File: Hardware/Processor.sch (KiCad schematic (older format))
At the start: 24 parts, among them J1 ICSP-CORTEX, J3 CONN-9, U6 STM32L100RBT6, X1 8MHz

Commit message: Component associations
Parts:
- removed R?: R, ~, symbol R
- added R18: 10k, RESC1608, symbol R
- gave numbers to parts that had none: 7
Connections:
- net +3.3V: now also R18.2
- net VLCD: now also R18.1
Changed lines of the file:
@@
 $EndComp
 $Comp
-L VCOM #PWR38
+L VCOM #PWR50
 U 1 1 52B50CC7
 P 9300 5500
-F 0 "#PWR38" H 9300 5700 40  0001 C CNN
+F 0 "#PWR50" H 9300 5700 40  0001 C CNN
 F 1 "VCOM" H 9300 5650 40  0000 C CNN
 F 2 "" H 9300 5500 60  0000 C CNN
@@
 LED0
 Wire Wire Line
-	2800 5100 2800 5200
-Wire Wire Line
-	2800 5200 2800 5300
-Wire Wire Line
-	2100 5100 2100 5200
-Wire Wire Line
-	2100 5200 2100 5300
+	2800 5100 2800 5300
+Wire Wire Line
+	2100 5100 2100 5300
 Wire Wire Line
 	2200 5200 2100 5200
@@
 	5700 3800 5600 3800
 Wire Wire Line
-	4400 3500 4400 3600
-Wire Wire Line
-	4400 3600 4400 3800
-Wire Wire Line
-	4400 3800 4400 4300
-Wire Wire Line
-	4400 4300 4400 4500
+	4400 3500 4400 4500
 Wire Wire Line
 	4400 4500 4500 4500
@@
 	2100 2200 2300 2200
 $Comp
-L C C?
+L C C50
 U 1 1 5411C9AD
 P 4300 6850
-F 0 "C?" H 4350 7000 60  0000 L CNN
+F 0 "C50" H 4350 7000 60  0000 L CNN
 F 1 "0.1uF" H 4350 6700 60  0000 L CNN
 F 2 "CAPC1608" H 4300 6850 60  0001 C CNN
@@
 $EndComp
 $Comp
-L C C?
+L C C48
 U 1 1 5411CA70
 P 1600 6850
-F 0 "C?" H 1650 7000 60  0000 L CNN
+F 0 "C48" H 1650 7000 60  0000 L CNN
 F 1 "1uF" H 1650 6700 60  0000 L CNN
 F 2 "CAPC1608" H 1600 6850 60  0001 C CNN
@@
 $EndComp
 $Comp
-L C C?
+L C C47
 U 1 1 5411CA9D
 P 1100 6850
-F 0 "C?" H 1150 7000 60  0000 L CNN
+F 0 "C47" H 1150 7000 60  0000 L CNN
 F 1 "0.1uF" H 1150 6700 60  0000 L CNN
 F 2 "CAPC1608" H 1100 6850 60  0001 C CNN
@@
 $EndComp
 $Comp
-L +3.3V #PWR?
+L +3.3V #PWR039
 U 1 1 5411CAA5
 P 2300 6400
-F 0 "#PWR?" H 2300 6360 30  0001 C CNN
+F 0 "#PWR039" H 2300 6360 30  0001 C CNN
 F 1 "+3.3V" H 2300 6510 30  0000 C CNN
 F 2 "" H 2300 6400 60  0000 C CNN
@@
 $EndComp
 Wire Wire Line
-	2300 6400 2300 6500
-Wire Wire Line
-	2300 6500 2300 6600
-$Comp
-L GND #PWR?
+	2300 6400 2300 6600
+$Comp
+L GND #PWR040
 U 1 1 5411CAE0
 P 2300 7200
-F 0 "#PWR?" H 2300 7200 30  0001 C CNN
+F 0 "#PWR040" H 2300 7200 30  0001 C CNN
 F 1 "GND" H 2300 7130 30  0001 C CNN
 F 2 "" H 2300 7200 60  0000 C CNN
@@
 $EndComp
 $Comp
-L GND #PWR?
+L GND #PWR041
 U 1 1 5411CAEF
 P 2800 7200
-F 0 "#PWR?" H 2800 7200 30  0001 C CNN
+F 0 "#PWR041" H 2800 7200 30  0001 C CNN
 F 1 "GND" H 2800 7130 30  0001 C CNN
 F 2 "" H 2800 7200 60  0000 C CNN
@@
 $EndComp
 $Comp
-L GND #PWR?
+L GND #PWR042
 U 1 1 5411CAFE
 P 3300 7200
-F 0 "#PWR?" H 3300 7200 30  0001 C CNN
+F 0 "#PWR042" H 3300 7200 30  0001 C CNN
 F 1 "GND" H 3300 7130 30  0001 C CNN
 F 2 "" H 3300 7200 60  0000 C CNN
@@
 $EndComp
 $Comp
-L GND #PWR?
+L GND #PWR043
 U 1 1 5411CB0D
 P 3800 7200
-F 0 "#PWR?" H 3800 7200 30  0001 C CNN
+F 0 "#PWR043" H 3800 7200 30  0001 C CNN
 F 1 "GND" H 3800 7130 30  0001 C CNN
 F 2 "" H 3800 7200 60  0000 C CNN
@@
 $EndComp
 $Comp
-L GND #PWR?
+L GND #PWR044
 U 1 1 5411CB1C
 P 4300 7200
-F 0 "#PWR?" H 4300 7200 30  0001 C CNN
+F 0 "#PWR044" H 4300 7200 30  0001 C CNN
 F 1 "GND" H 4300 7130 30  0001 C CNN
 F 2 "" H 4300 7200 60  0000 C CNN
@@
 $EndComp
 $Comp
-L GND #PWR?
+L GND #PWR045
 U 1 1 5411CB2B
 P 1600 7200
-F 0 "#PWR?" H 1600 7200 30  0001 C CNN
+F 0 "#PWR045" H 1600 7200 30  0001 C CNN
 F 1 "GND" H 1600 7130 30  0001 C CNN
 F 2 "" H 1600 7200 60  0000 C CNN
@@
 $EndComp
 $Comp
-L GND #PWR?
+L GND #PWR046
 U 1 1 5411CB3A
 P 1100 7200
-F 0 "#PWR?" H 1100 7200 30  0001 C CNN
+F 0 "#PWR046" H 1100 7200 30  0001 C CNN
 F 1 "GND" H 1100 7130 30  0001 C CNN
 F 2 "" H 1100 7200 60  0000 C CNN
@@
 $EndComp
 Wire Wire Line
-	1100 6400 1100 6500
-Wire Wire Line
-	1100 6500 1100 6600
+	1100 6400 1100 6600
 Connection ~ 2300 6500
 Wire Wire Line
@@
 	4300 7100 4300 7200
 $Comp
-L R R?
-U 1 1 5411CE1B
-P 4650 6500
-F 0 "R?" H 4650 6600 50  0000 C CNN
-F 1 "R" H 4650 6500 50  0000 C CNN
-F 2 "~" H 4650 6500 60  0000 C CNN
-F 3 "~" H 4650 6500 60  0000 C CNN
-F 4 "W" H 4650 6400 50  0001 C CNN "Power"
-F 5 "%" H 4650 6300 50  0001 C CNN "Tolerance"
-	1    4650 6500
-	1    0    0    -1
-$EndComp
-$Comp
-L C C?
+L C C51
 U 1 1 5411CE39
 P 5000 6850
-F 0 "C?" H 5050 7000 60  0000 L CNN
+F 0 "C51" H 5050 7000 60  0000 L CNN
 F 1 "0.1uF" H 5050 6700 60  0000 L CNN
 F 2 "CAPC1608" H 5000 6850 60  0001 C CNN
@@
 Connection ~ 4300 6500
 Wire Wire Line
-	4900 6500 5000 6500
-Wire Wire Line
-	5000 6500 5100 6500
+	4900 6500 5100 6500
 Wire Wire Line
 	5000 6500 5000 6600
 $Comp
-L GND #PWR?
+L GND #PWR047
 U 1 1 5411CEC2
 P 5000 7200
-F 0 "#PWR?" H 5000 7200 30  0001 C CNN
+F 0 "#PWR047" H 5000 7200 30  0001 C CNN
 F 1 "GND" H 5000 7130 30  0001 C CNN
 F 2 "" H 5000 7200 60  0000 C CNN
@@
 Connection ~ 5000 6500
 Wire Wire Line
-	1100 6500 1600 6500
-Wire Wire Line
-	1600 6500 1700 6500
-Wire Wire Line
-	2200 6500 2300 6500
-Wire Wire Line
-	2300 6500 2800 6500
-Wire Wire Line
-	2800 6500 3300 6500
-Wire Wire Line
-	3300 6500 3800 6500
-Wire Wire Line
-	3800 6500 4300 6500
-Wire Wire Line
-	4300 6500 4400 6500
-$Comp
-L FERRITE FB?
+	1100 6500 1700 6500
+Wire Wire Line
+	2200 6500 4400 6500
+$Comp
+L FERRITE FB1
 U 1 1 5411CFE1
 P 1950 6500
-F 0 "FB?" H 1900 6550 60  0000 R CNN
+F 0 "FB1" H 1900 6550 60  0000 R CNN
 F 1 "FERRITE" H 2000 6450 60  0000 L CNN
 F 2 "~" H 1950 6500 60  0000 C CNN
@@
 $EndComp
 $Comp
-L +3.3VADC #PWR?
+L +3.3VADC #PWR048
 U 1 1 5411D0AC
 P 1100 6400
-F 0 "#PWR?" H 1100 6520 20  0001 C CNN
+F 0 "#PWR048" H 1100 6520 20  0001 C CNN
 F 1 "+3.3VADC" H 1100 6490 30  0000 C CNN
 F 2 "" H 1100 6400 60  0000 C CNN
@@
 Connection ~ 1100 6500
 $Comp
-L +3.3VADC #PWR?
+L +3.3VADC #PWR049
 U 1 1 5411D101
 P 10300 2700
-F 0 "#PWR?" H 10300 2820 20  0001 C CNN
+F 0 "#PWR049" H 10300 2820 20  0001 C CNN
 F 1 "+3.3VADC" H 10300 2790 30  0000 C CNN
 F 2 "" H 10300 2700 60  0000 C CNN
@@
 $EndComp
 $Comp
-L +3.3V #PWR?
+L +3.3V #PWR050
 U 1 1 5411D110
 P 10100 2700
-F 0 "#PWR?" H 10100 2660 30  0001 C CNN
+F 0 "#PWR050" H 10100 2660 30  0001 C CNN
 F 1 "+3.3V" H 10100 2810 30  0000 C CNN
 F 2 "" H 10100 2700 60  0000 C CNN
@@
 $EndComp
 Wire Wire Line
-	10100 2700 10100 3400
-Wire Wire Line
-	10100 3400 10100 3500
-Wire Wire Line
-	10100 3500 10100 3600
-Wire Wire Line
-	10100 3600 10100 3700
+	10100 2700 10100 3700
 Wire Wire Line
 	10100 3400 10000 3400
@@
 	10400 3300 10000 3300
 $Comp
-L GND #PWR?
+L GND #PWR051
 U 1 1 5411D2E7
 P 10100 4400
-F 0 "#PWR?" H 10100 4400 30  0001 C CNN
+F 0 "#PWR051" H 10100 4400 30  0001 C CNN
 F 1 "GND" H 10100 4330 30  0001 C CNN
 F 2 "" H 10100 4400 60  0000 C CNN
@@
 $EndComp
 Wire Wire Line
-	10100 3900 10100 4000
-Wire Wire Line
-	10100 4000 10100 4100
-Wire Wire Line
-	10100 4100 10100 4200
-Wire Wire Line
-	10100 4200 10100 4300
-Wire Wire Line
-	10100 4300 10100 4400
+	10100 3900 10100 4400
 Wire Wire Line
 	10100 3900 10000 3900
@@
 NoConn ~ 10000 3200
 $Comp
-L C C?
+L C C49
 U 1 1 5411D10E
 P 3000 2150
-F 0 "C?" H 3050 2300 60  0000 L CNN
+F 0 "C49" H 3050 2300 60  0000 L CNN
 F 1 "0.1uF" H 3050 2000 60  0000 L CNN
 F 2 "CAPC1608" H 3000 2150 60  0001 C CNN
@@
 ~RST
 $Comp
-L GND #PWR?
+L GND #PWR052
 U 1 1 5411D116
 P 3000 2500
-F 0 "#PWR?" H 3000 2500 30  0001 C CNN
+F 0 "#PWR052" H 3000 2500 30  0001 C CNN
 F 1 "GND" H 3000 2430 30  0001 C CNN
 F 2 "" H 3000 2500 60  0000 C CNN
@@
 	3000 1900 3000 1800
 $Comp
-L R R?
+L R R12
 U 1 1 5411D395
 P 3600 2150
-F 0 "R?" H 3600 2250 50  0000 C CNN
+F 0 "R12" H 3600 2250 50  0000 C CNN
 F 1 "10k" H 3600 2150 50  0000 C CNN
 F 2 "RESC1608" H 3600 2150 60  0001 C CNN
@@
 $EndComp
 $Comp
-L GND #PWR?
+L GND #PWR053
 U 1 1 5411D3B1
 P 3600 2500
-F 0 "#PWR?" H 3600 2500 30  0001 C CNN
+F 0 "#PWR053" H 3600 2500 30  0001 C CNN
 F 1 "GND" H 3600 2430 30  0001 C CNN
 F 2 "" H 3600 2500 60  0000 C CNN
@@
 Wire Wire Line
 	7400 2200 7600 2200
+$Comp
+L R R18
+U 1 1 5411D7D0
+P 4650 6500
+F 0 "R18" H 4650 6600 50  0000 C CNN
+F 1 "10k" H 4650 6500 50  0000 C CNN
+F 2 "RESC1608" H 4650 6500 60  0001 C CNN
+F 3 "~" H 4650 6500 60  0000 C CNN
+F 4 "Yageo" H 4650 6500 60  0001 C CNN "MFR Name"
+F 5 "RC0603FR-0710KL" H 4650 6500 60  0001 C CNN "MFR Part No"
+F 6 "311-10.0KHRCT-ND" H 4650 6500 60  0001 C CNN "Distributor Part No"
+F 7 "0.1W" H 4650 6400 50  0001 C CNN "Power"
+F 8 "1%" H 4650 6300 50  0001 C CNN "Tolerance"
+	1    4650 6500
+	-1   0    0    -1
+$EndComp
 $EndSCHEMATC

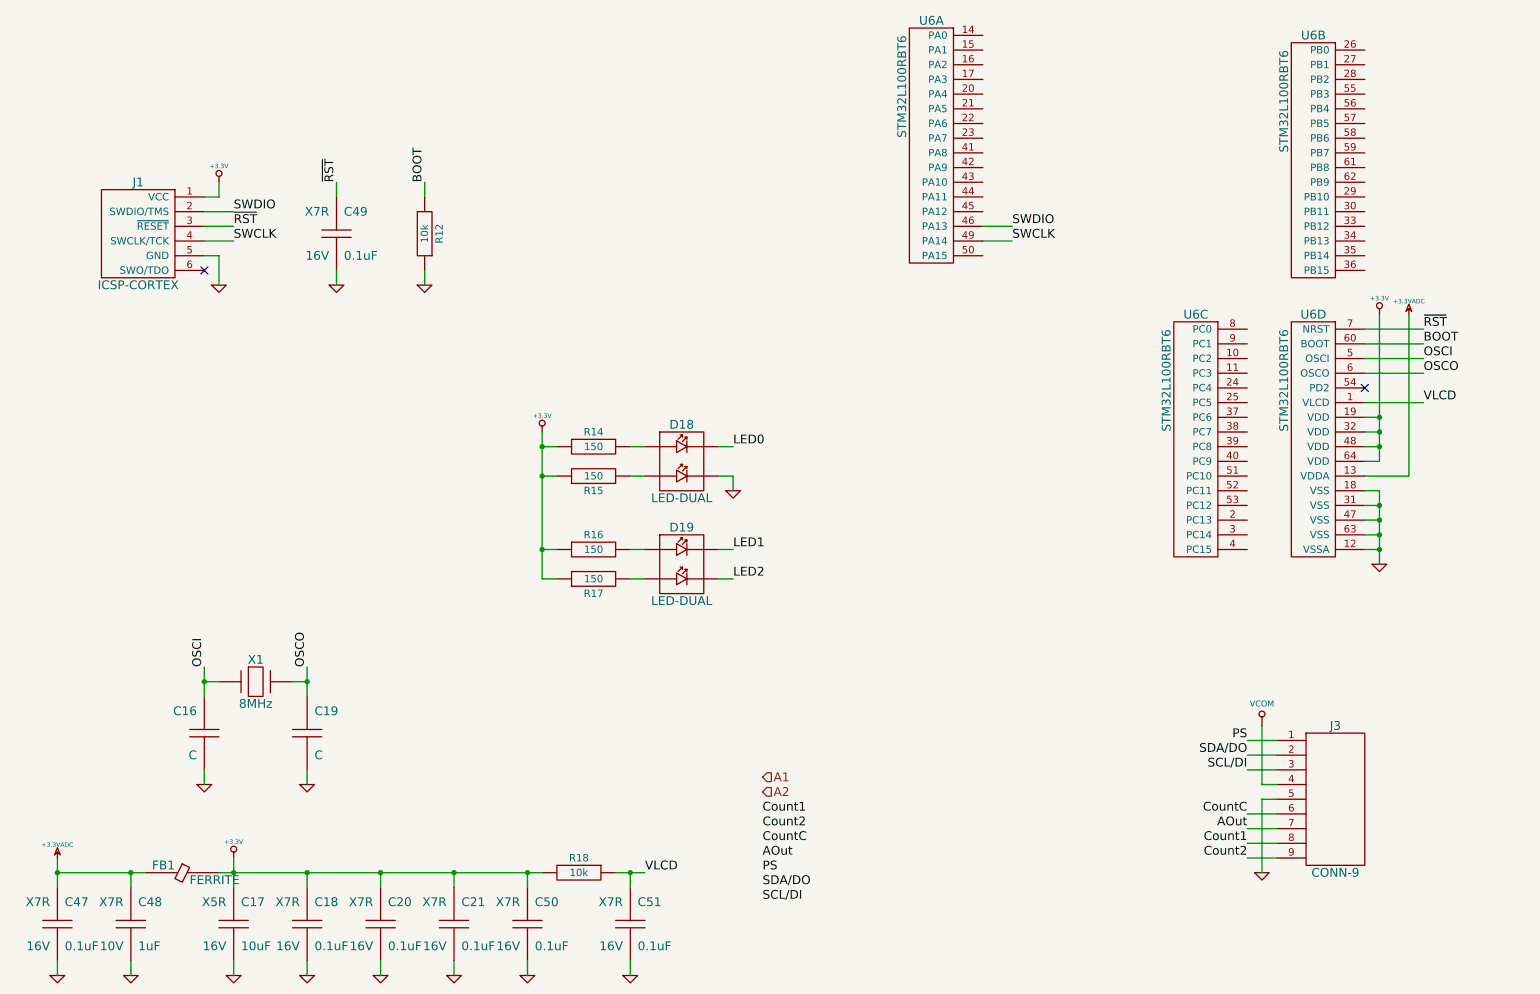
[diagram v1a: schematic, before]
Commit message: Add threshold detector
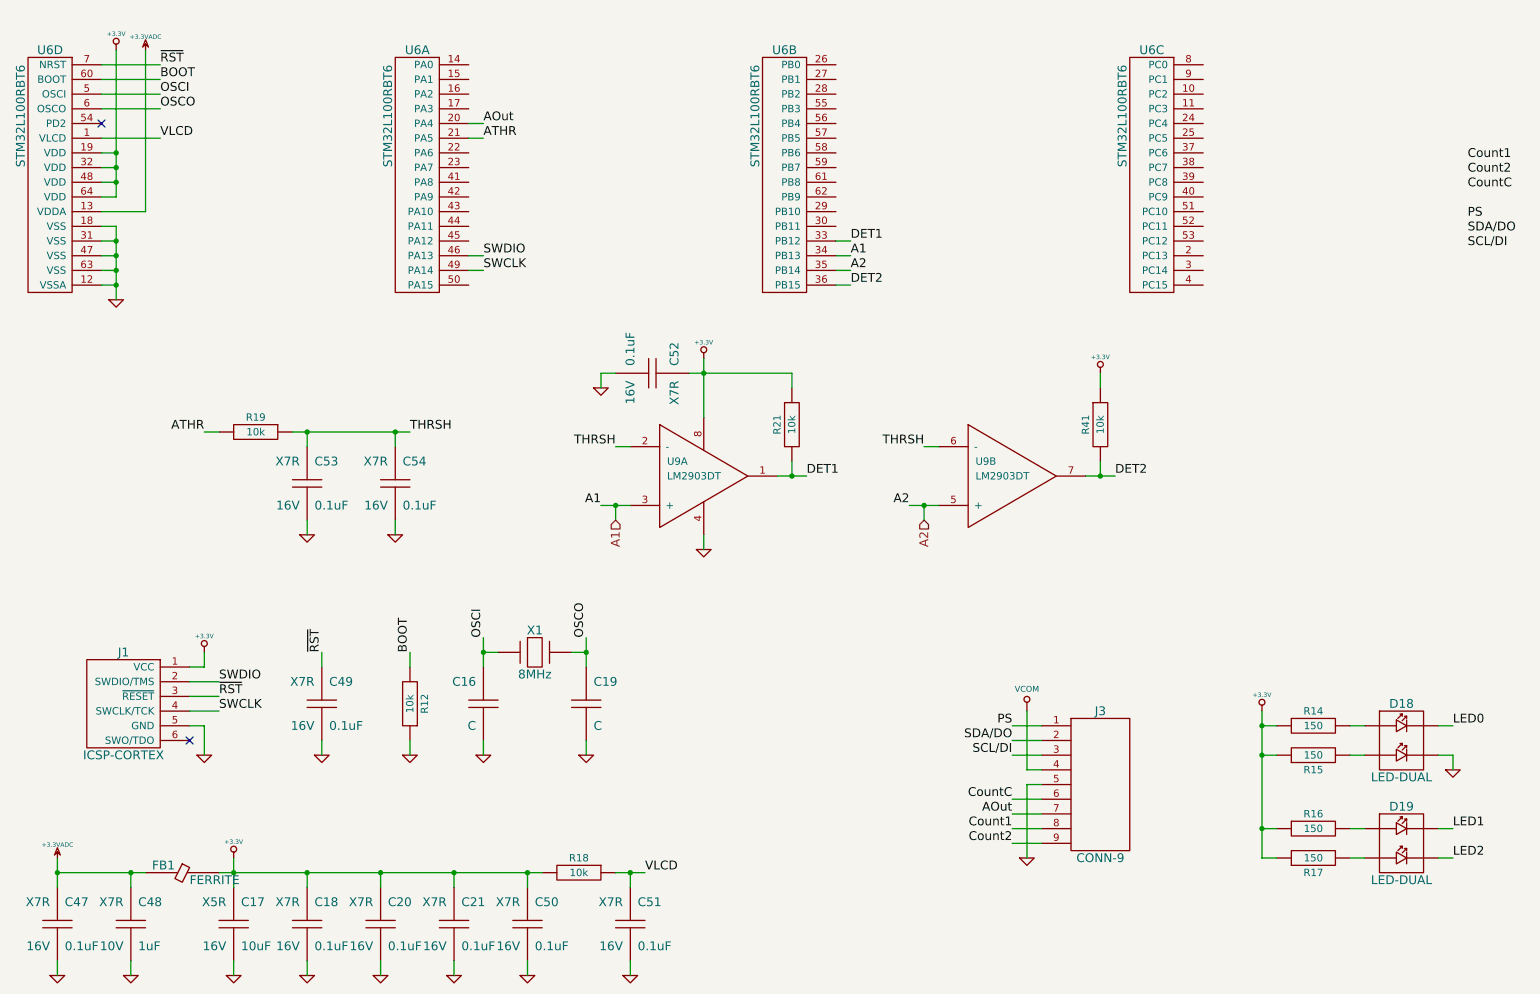
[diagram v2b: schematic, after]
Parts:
- added C52, C53, C54: 0.1uF, CAPC1608, symbol C
- added R19, R21, R41: 10k, RESC1608, symbol R
- added U9: LM2903DT, ~, symbol OPAMP-DUAL
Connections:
- net +3.3V: now also C52.1, R21.1, R41.1, U9.8
- net A1: now also U6.34 (PB13), U9.3 (+)
- net A2: now also U6.35 (PB14), U9.5 (+)
- net AOut: now also U6.20 (PA4)
- net GND: now also C52.2, C53.2, C54.2, U9.4
- net ATHR: now reaches U6.21 (PA5)
- net ATHR: now also R19.2
- net DET1: now reaches U6.33 (PB12)
- net DET1: now also R21.2, U9.1
- net DET2: now reaches U6.36 (PB15)
- net DET2: now also R41.2, U9.7
- new net THRSH: C53.1, C54.1, R19.1, U9.2 (-), U9.6 (-)
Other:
- moved on the sheet: C16, C19, C49, D18, D19, J1, J3, R12, R14, R15, R16, R17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

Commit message: Change DB9 to in stock part
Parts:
- J3: Distributor Part No A35107-ND -> A35108-ND; MFR Part No 1734354-1 -> 1734354-2
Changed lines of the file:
@@
 F 3 "~" H 8200 5950 60  0000 C CNN
 F 4 "TE" H 8200 5900 60  0001 C CNN "MFR Name"
-F 5 "1734354-1" H 8200 5900 60  0001 C CNN "MFR Part No"
-F 6 "A35107-ND" H 8200 5900 60  0001 C CNN "Distributor Part No"
+F 5 "1734354-2" H 8200 5900 60  0001 C CNN "MFR Part No"
+F 6 "A35108-ND" H 8200 5900 60  0001 C CNN "Distributor Part No"
 	1    8200 5900
 	-1   0    0    -1
